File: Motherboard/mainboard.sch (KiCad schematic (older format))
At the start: 53 parts, among them IC1 BMX160, J1 Conn_01x01, J2 10118194-0001LF, J28 Conn_01x01, J29 Conn_01x01, J3 Micro_SD_Card, J30 Conn_01x01, J4 xf2m-2415-1a, J5 XF2M-1015-1A, J6 U.FL-R-SMT-1, J7 U.FL-R-SMT-1, J8 Conn_01x01, J9 XF2M36151A, SW1 KMR231NG LFS, U1 RFM95W-915S2, U2 ATSAMD51G_TQFN48, U3 DRV8848, U4 TPS82740BSIPR, U5 DRV8848, U6 MAX708RESA-T, U8 RFM95W-915S2

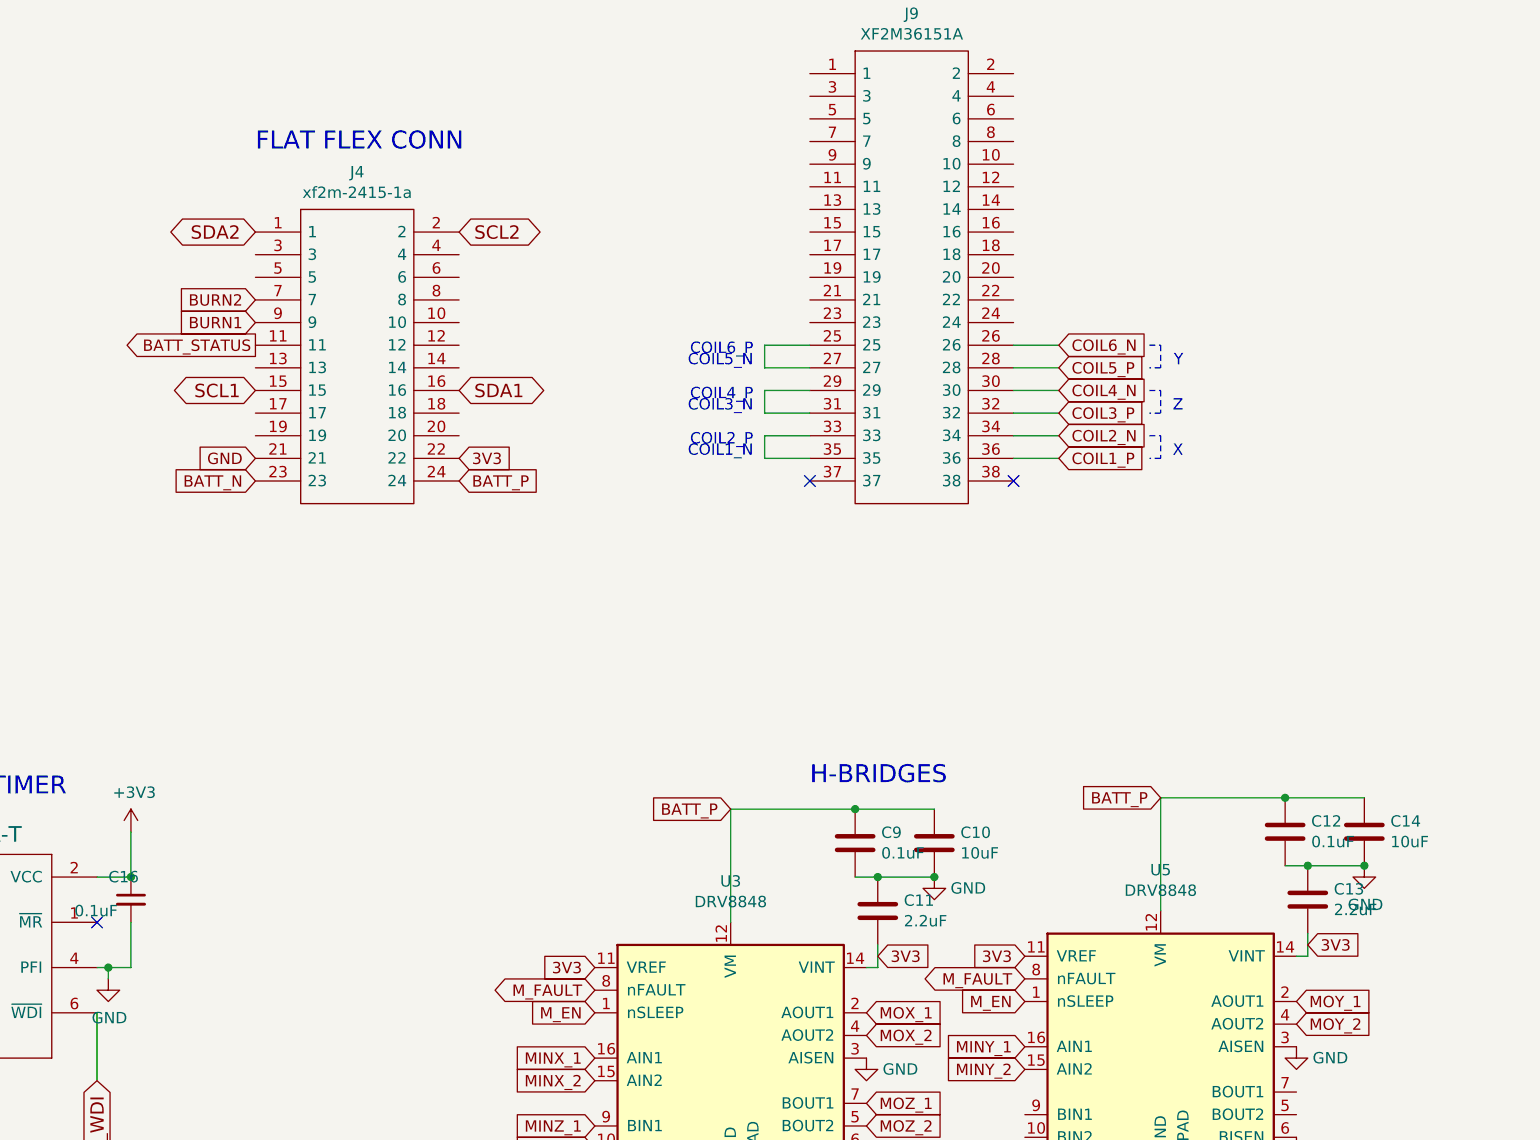
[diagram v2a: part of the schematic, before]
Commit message: coil bridges with contingency finished
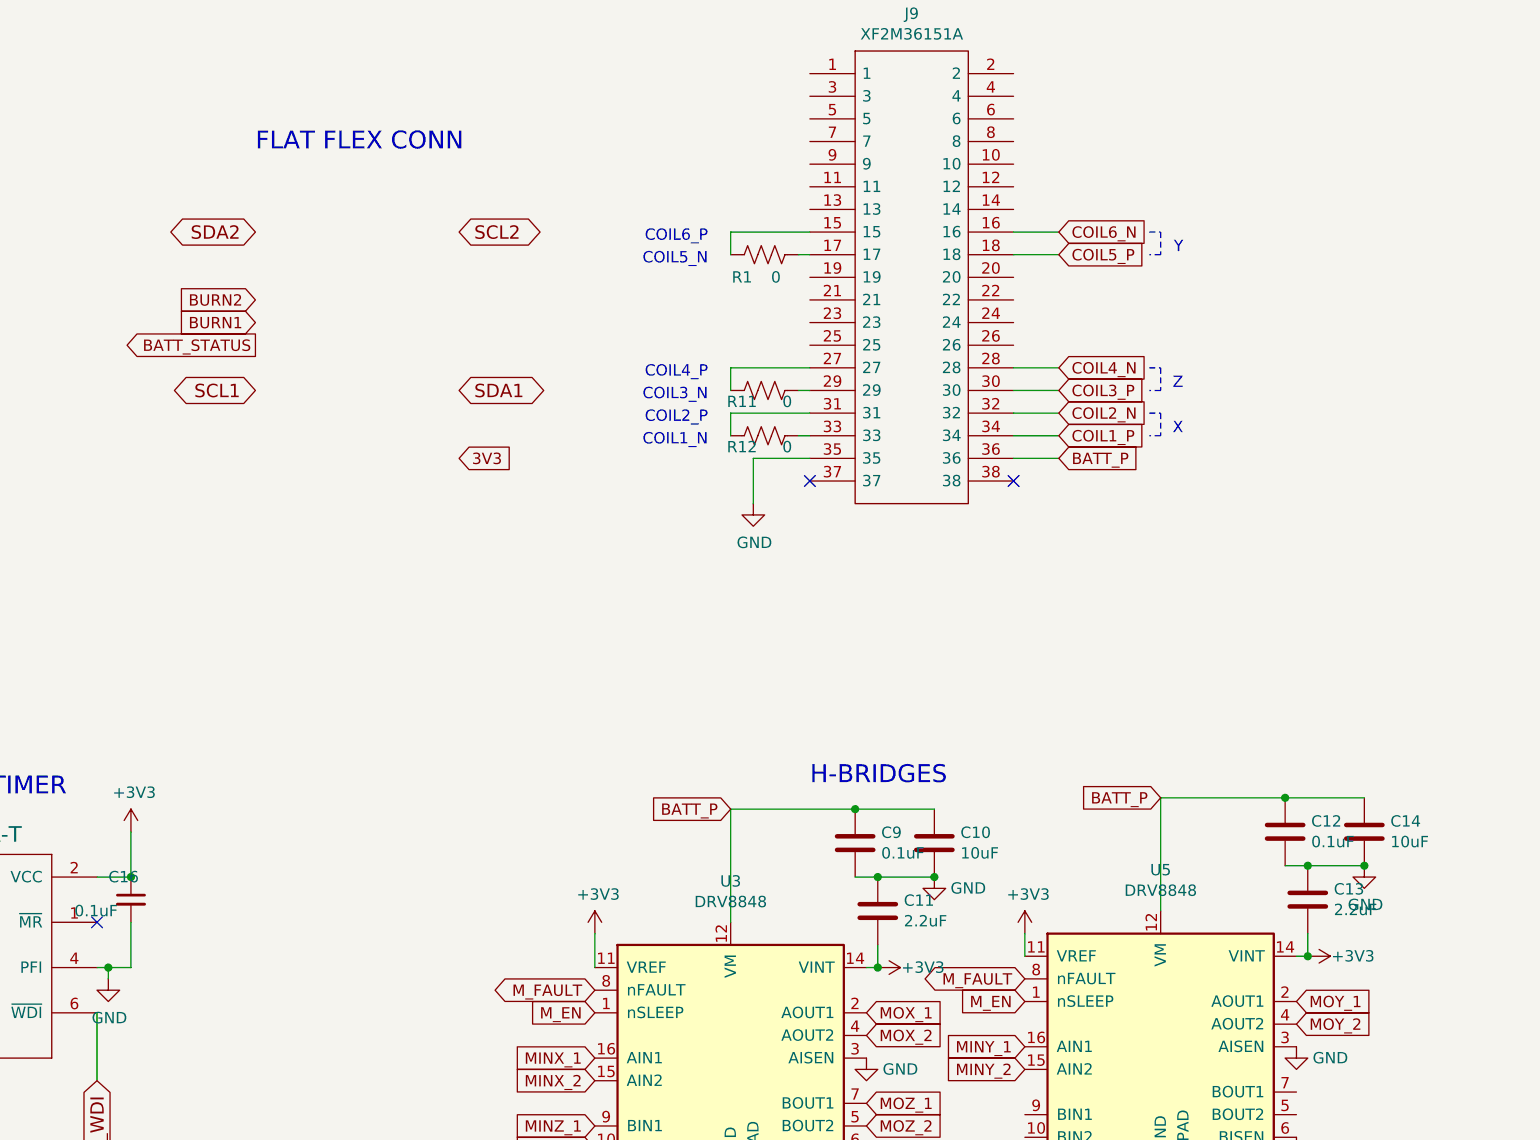
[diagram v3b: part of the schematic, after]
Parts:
- removed J4: xf2m-2415-1a, custom-footprints:XF2M-2415-1A, symbol mainboard-rescue:xf2m-2415-1a-symbols
- added R1, R11, R12: 0, Resistor_SMD:R_0402_1005Metric, symbol mainboard-rescue:R_US-Device
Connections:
- net +3V3: now also C11.2, C13.2, U3.11 (VREF), U3.14 (VINT), U5.11 (VREF), U5.14 (VINT)
- net 3V3: no longer C11.2, C13.2, U3.11 (VREF), U3.14 (VINT), U5.11 (VREF), U5.14 (VINT)
- net BATT_P: now also J9.36
- net COIL1_P: now also J9.34; no longer J9.36
- net COIL2_N: now also J9.32; no longer J9.34
- net COIL3_P: now also J9.30; no longer J9.32
- net COIL4_N: now also J9.28; no longer J9.30
- net COIL5_P: now also J9.18; no longer J9.28
- net COIL6_N: now also J9.16; no longer J9.26
- net GND: now also J9.35
- net at J9.15: now also R1.1
- net at J9.17: now also R1.2
- net at J9.25: no longer J9.27
- net at J9.29: now also R11.2; no longer J9.31
- net at J9.33: now also R12.2; no longer J9.35
- new net: J9.27, R11.1
- new net: J9.31, R12.1
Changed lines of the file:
@@
 	10000 4200 9900 4200
-$Comp
-L mainboard-rescue:xf2m-2415-1a-symbols J4
-U 1 1 5DBA91E1
-P 5400 -1800
-F 0 "J4" H 5850 -1535 50  0000 C CNN
-F 1 "xf2m-2415-1a" H 5850 -1626 50  0000 C CNN
-F 2 "custom-footprints:XF2M-2415-1A" H 6150 -1700 50  0001 L CNN
-F 3 "http://docs-emea.rs-online.com/webdocs/0fd2/0900766b80fd28a0.pdf" H 6150 -1800 50  0001 L CNN
-F 4 "Omron XF2M Series 0.5mm Pitch 24 Way 1 Row Right Angle SMT Female FPC Connector Locking Mechanism, Gold Plated Contacts" H 6150 -1900 50  0001 L CNN "Description"
-	1    5400 -1800
-	1    0    0    -1
-$EndComp
 $Comp
 L mainboard-rescue:MAX708RESA-T-symbols U6
@@
 Text GLabel 6300 -800 2    50   Input ~ 0
 3V3
-Text GLabel 5400 -800 0    50   Input ~ 0
-GND
-Text GLabel 6300 -700 2    50   Input ~ 0
+Text GLabel 8950 -800 2    50   Input ~ 0
 BATT_P
-Text GLabel 5400 -700 0    50   Input ~ 0
-BATT_N
 Text GLabel 5400 -1400 0    50   Input ~ 0
 BURN1
 Text GLabel 5400 -1500 0    50   Input ~ 0
 BURN2
-Text GLabel 8950 -800 2    50   Input ~ 0
+Text GLabel 8950 -900 2    50   Input ~ 0
 COIL1_P
 Wire Wire Line
@@
 Wire Wire Line
 	4750 1450 4750 1500
-Text GLabel 8950 -1000 2    50   Input ~ 0
+Text GLabel 8950 -1100 2    50   Input ~ 0
 COIL3_P
 Text GLabel 5300 5900 2    59   BiDi ~ 0
@@
 Text GLabel 9400 700  0    50   Input ~ 0
 BATT_P
-Text GLabel 6900 1450 0    50   Input ~ 0
-3V3
-Text GLabel 8150 1400 2    50   Input ~ 0
-3V3
-Text GLabel 8800 1400 0    50   Input ~ 0
-3V3
-Text GLabel 10050 1350 2    50   Input ~ 0
-3V3
 $Comp
 L mainboard-rescue:C_Small-Device C15
@@
 NoConn ~ 8750 -700
 NoConn ~ 7850 -700
-Text GLabel 8950 -1100 2    50   Input ~ 0
+Text GLabel 8950 -1200 2    50   Input ~ 0
 COIL4_N
 Wire Wire Line
-	7850 -900 7650 -900
-Wire Wire Line
-	7650 -900 7650 -800
-Wire Wire Line
-	7650 -800 7850 -800
-Text Notes 7600 -800 2    50   ~ 0
+	7800 -900 7850 -900
+Text Notes 7400 -850 2    50   ~ 0
 COIL1_N
-Wire Wire Line
-	7850 -1000 7650 -1000
-Wire Wire Line
-	7650 -1000 7650 -1100
-Wire Wire Line
-	7650 -1100 7850 -1100
-Text Notes 7600 -1000 2    50   ~ 0
+Text Notes 7400 -1050 2    50   ~ 0
 COIL3_N
-Text GLabel 8950 -1200 2    50   Input ~ 0
+Text GLabel 8950 -1700 2    50   Input ~ 0
 COIL5_P
 Wire Wire Line
-	7850 -1300 7650 -1300
-Wire Wire Line
-	7650 -1300 7650 -1200
-Wire Wire Line
-	7650 -1200 7850 -1200
-Wire Wire Line
-	8750 -800 8950 -800
-Text GLabel 8950 -900 2    50   Input ~ 0
+	8750 -900 8950 -900
+Text GLabel 8950 -1000 2    50   Input ~ 0
 COIL2_N
 Wire Wire Line
-	8950 -900 8750 -900
-Text Notes 7600 -850 2    50   ~ 0
+	8950 -1000 8750 -1000
+Text Notes 7400 -950 2    50   ~ 0
 COIL2_P
-Text Notes 7600 -1050 2    50   ~ 0
+Text Notes 7400 -1150 2    50   ~ 0
 COIL4_P
-Text Notes 7600 -1200 2    50   ~ 0
+Text Notes 7400 -1650 2    50   ~ 0
 COIL5_N
-Text Notes 7600 -1250 2    50   ~ 0
+Text Notes 7400 -1750 2    50   ~ 0
 COIL6_P
 Wire Wire Line
-	8750 -1200 8950 -1200
-Wire Wire Line
-	8750 -1000 8950 -1000
-Wire Wire Line
-	8950 -1100 8750 -1100
-Text GLabel 8950 -1300 2    50   Input ~ 0
+	8750 -1700 8950 -1700
+Wire Wire Line
+	8750 -1100 8950 -1100
+Wire Wire Line
+	8950 -1200 8750 -1200
+Text GLabel 8950 -1800 2    50   Input ~ 0
 COIL6_N
 Wire Wire Line
-	8950 -1300 8750 -1300
+	8950 -1800 8750 -1800
 Wire Notes Line
-	9350 -900 9400 -900
+	9350 -1000 9400 -1000
 Wire Notes Line
-	9400 -900 9400 -800
+	9400 -1000 9400 -900
 Wire Notes Line
-	9400 -800 9350 -800
+	9400 -900 9350 -900
 Wire Notes Line
-	9350 -1100 9400 -1100
+	9350 -1200 9400 -1200
 Wire Notes Line
-	9400 -1100 9400 -1000
+	9400 -1200 9400 -1100
 Wire Notes Line
-	9400 -1000 9350 -1000
+	9400 -1100 9350 -1100
 Wire Notes Line
-	9350 -1300 9400 -1300
+	9350 -1800 9400 -1800
 Wire Notes Line
-	9400 -1300 9400 -1200
+	9400 -1800 9400 -1700
 Wire Notes Line
-	9400 -1200 9350 -1200
-Text Notes 9500 -1200 2    50   ~ 0
+	9400 -1700 9350 -1700
+Text Notes 9500 -1700 2    50   ~ 0
 Y
-Text Notes 9500 -1000 2    50   ~ 0
+Text Notes 9500 -1100 2    50   ~ 0
 Z
-Text Notes 9500 -800 2    50   ~ 0
+Text Notes 9500 -900 2    50   ~ 0
 X
+$Comp
+L mainboard-rescue:R_US-Device R12
+U 1 1 5DE2535B
+P 7650 -900
+F 0 "R12" V 7600 -800 50  0000 C CNN
+F 1 "0" V 7600 -1000 50  0000 C CNN
+F 2 "Resistor_SMD:R_0402_1005Metric" V 7690 -910 50  0001 C CNN
+F 3 "~" H 7650 -900 50  0001 C CNN
+	1    7650 -900
+	0    -1   -1   0
+$EndComp
+Wire Wire Line
+	7500 -1000 7500 -900
+Wire Wire Line
+	7500 -1000 7850 -1000
+Wire Wire Line
+	7800 -1100 7850 -1100
+$Comp
+L mainboard-rescue:R_US-Device R11
+U 1 1 5DE4E3AF
+P 7650 -1100
+F 0 "R11" V 7600 -1000 50  0000 C CNN
+F 1 "0" V 7600 -1200 50  0000 C CNN
+F 2 "Resistor_SMD:R_0402_1005Metric" V 7690 -1110 50  0001 C CNN
+F 3 "~" H 7650 -1100 50  0001 C CNN
+	1    7650 -1100
+	0    -1   -1   0
+$EndComp
+Wire Wire Line
+	7500 -1200 7500 -1100
+Wire Wire Line
+	7500 -1200 7850 -1200
+Wire Wire Line
+	7800 -1700 7850 -1700
+$Comp
+L mainboard-rescue:R_US-Device R1
+U 1 1 5DE5629A
+P 7650 -1700
+F 0 "R1" V 7550 -1600 50  0000 C CNN
+F 1 "0" V 7550 -1750 50  0000 C CNN
+F 2 "Resistor_SMD:R_0402_1005Metric" V 7690 -1710 50  0001 C CNN
+F 3 "~" H 7650 -1700 50  0001 C CNN
+	1    7650 -1700
+	0    -1   -1   0
+$EndComp
+Wire Wire Line
+	7500 -1800 7500 -1700
+Wire Wire Line
+	7500 -1800 7850 -1800
+Wire Wire Line
+	8950 -800 8750 -800
+Wire Wire Line
+	7850 -800 7600 -800
+Wire Wire Line
+	7600 -800 7600 -600
+$Comp
+L power:GND #PWR0142
+U 1 1 5DF5F56B
+P 7600 -600
+F 0 "#PWR0142" H 7600 -850 50  0001 C CNN
+F 1 "GND" H 7605 -773 50  0000 C CNN
+F 2 "" H 7600 -600 50  0001 C CNN
+F 3 "" H 7600 -600 50  0001 C CNN
+	1    7600 -600
+	1    0    0    -1
+$EndComp
+$Comp
+L power:+3V3 #PWR0143
+U 1 1 5DF975F8
+P 10050 1400
+F 0 "#PWR0143" H 10050 1250 50  0001 C CNN
+F 1 "+3V3" V 10050 1600 50  0000 C CNN
+F 2 "" H 10050 1400 50  0001 C CNN
+F 3 "" H 10050 1400 50  0001 C CNN
+	1    10050 1400
+	0    1    1    0
+$EndComp
+Connection ~ 10050 1400
+$Comp
+L power:+3V3 #PWR0144
+U 1 1 5DFA15A8
+P 8150 1450
+F 0 "#PWR0144" H 8150 1300 50  0001 C CNN
+F 1 "+3V3" V 8150 1650 50  0000 C CNN
+F 2 "" H 8150 1450 50  0001 C CNN
+F 3 "" H 8150 1450 50  0001 C CNN
+	1    8150 1450
+	0    1    1    0
+$EndComp
+Connection ~ 8150 1450
+$Comp
+L power:+3V3 #PWR0145
+U 1 1 5DFA3E75
+P 6900 1300
+F 0 "#PWR0145" H 6900 1150 50  0001 C CNN
+F 1 "+3V3" H 6915 1473 50  0000 C CNN
+F 2 "" H 6900 1300 50  0001 C CNN
+F 3 "" H 6900 1300 50  0001 C CNN
+	1    6900 1300
+	1    0    0    -1
+$EndComp
+Wire Wire Line
+	6900 1300 6900 1450
+$Comp
+L power:+3V3 #PWR0146
+U 1 1 5DFAD179
+P 8800 1300
+F 0 "#PWR0146" H 8800 1150 50  0001 C CNN
+F 1 "+3V3" H 8815 1473 50  0000 C CNN
+F 2 "" H 8800 1300 50  0001 C CNN
+F 3 "" H 8800 1300 50  0001 C CNN
+	1    8800 1300
+	1    0    0    -1
+$EndComp
+Wire Wire Line
+	8800 1300 8800 1400
 $EndSCHEMATC
